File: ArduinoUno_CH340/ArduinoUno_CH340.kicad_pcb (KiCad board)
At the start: 2 copper layers, 68.6 x 53.3 mm, 63 parts, among them J1 Jack_DC, J10 ANALOG, J11 IOL, J2 USB_B, J3 Header_4P, J4 RxTx, J5 I2C, J6 Servo, J7 POWER, J8 ICSPx, J9 IOH, Q1 MOS-P_FDN304P, U1 MC33269-SOT, U2 CH340G, U3 LM358D, U4 ATmega328-P, U5 LP2985-3.3, Y1 16MHz, Y2 16MHz, Y3 16MHz

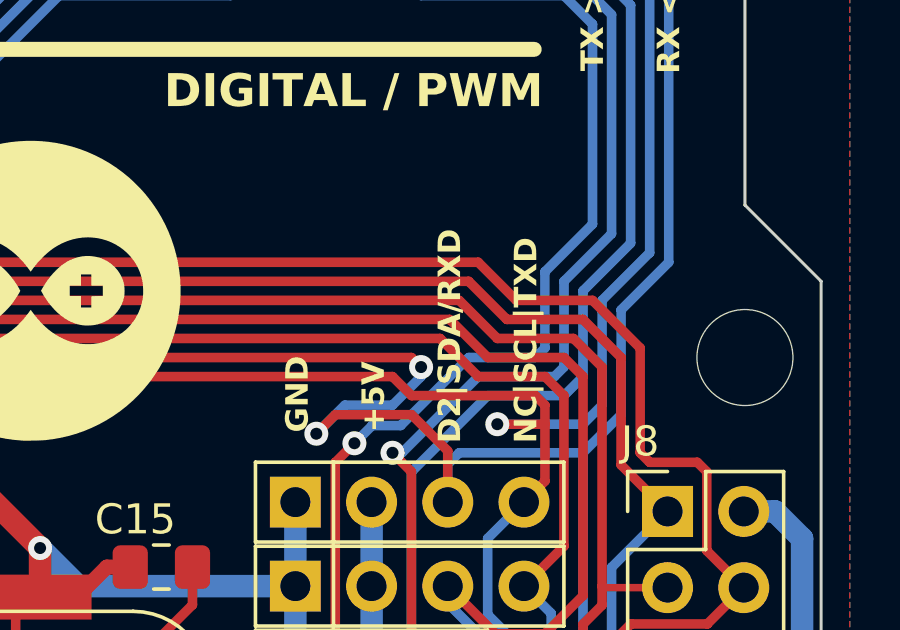
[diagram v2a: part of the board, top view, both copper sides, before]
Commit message: Complete Segmen595
Create New trial project for 7 Segmen + HC595
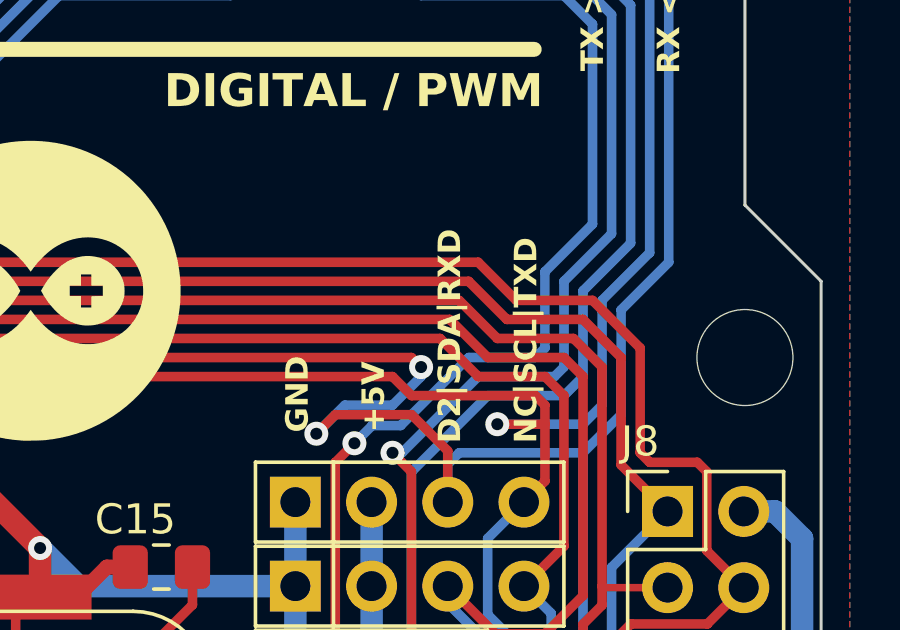
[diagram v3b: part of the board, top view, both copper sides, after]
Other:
- board text added: "D2|SDA|RXD"
- board text removed: "D2|SDA/RXD"
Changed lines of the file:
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@@
     (effects (font (size 0.75 0.75) (thickness 0.125) bold) (justify left))
   )
-  (gr_text "D2|SDA/RXD" (at 233.68 87.63 90) (layer "F.SilkS" knockout)
+  (gr_text "D2|SDA|RXD" (at 233.68 87.63 90) (layer "F.SilkS" knockout)
     (effects (font (size 0.75 0.75) (thickness 0.125) bold) (justify left))
   )
